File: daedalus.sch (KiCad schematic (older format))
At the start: 106 parts, among them J1 CAN Bus, J2 CAN Bus, J3 I2C 1 Breakout, J4 I2C 1 Breakout, J5 A Terminal, J6 B Terminal, J7 C Terminal, J8 SWD, J9 USB_B_Micro, Q1 AO3401A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

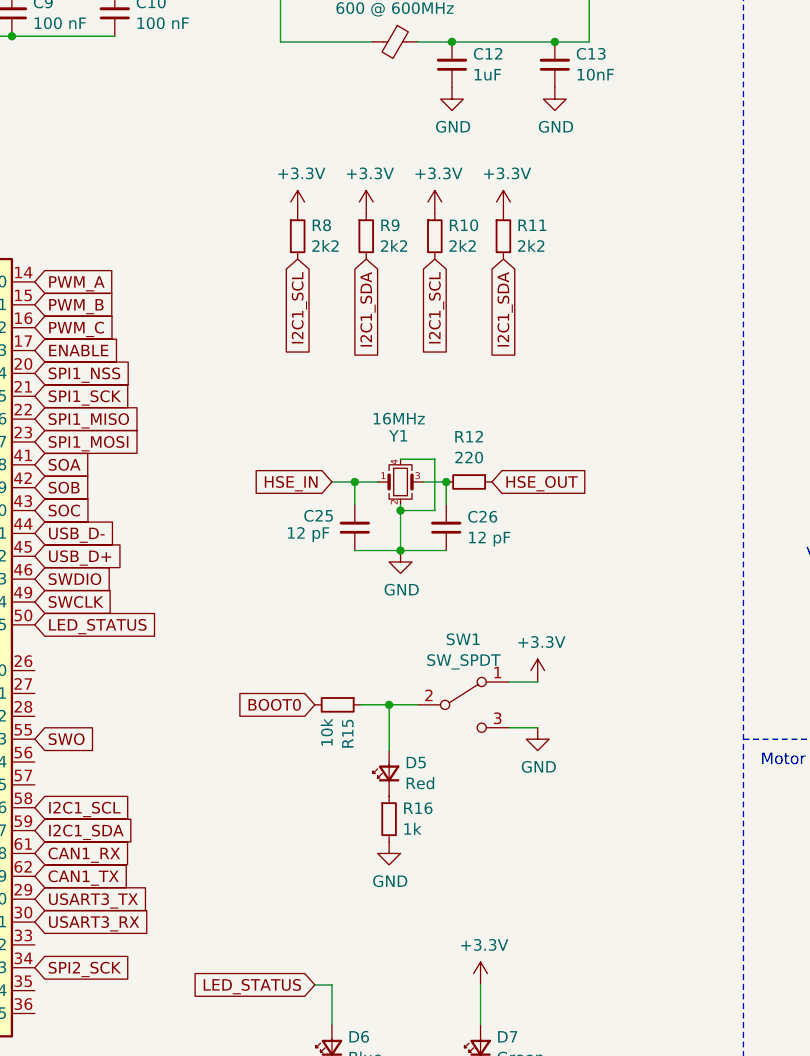
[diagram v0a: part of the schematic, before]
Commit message: Began sample routing, removed boot switch
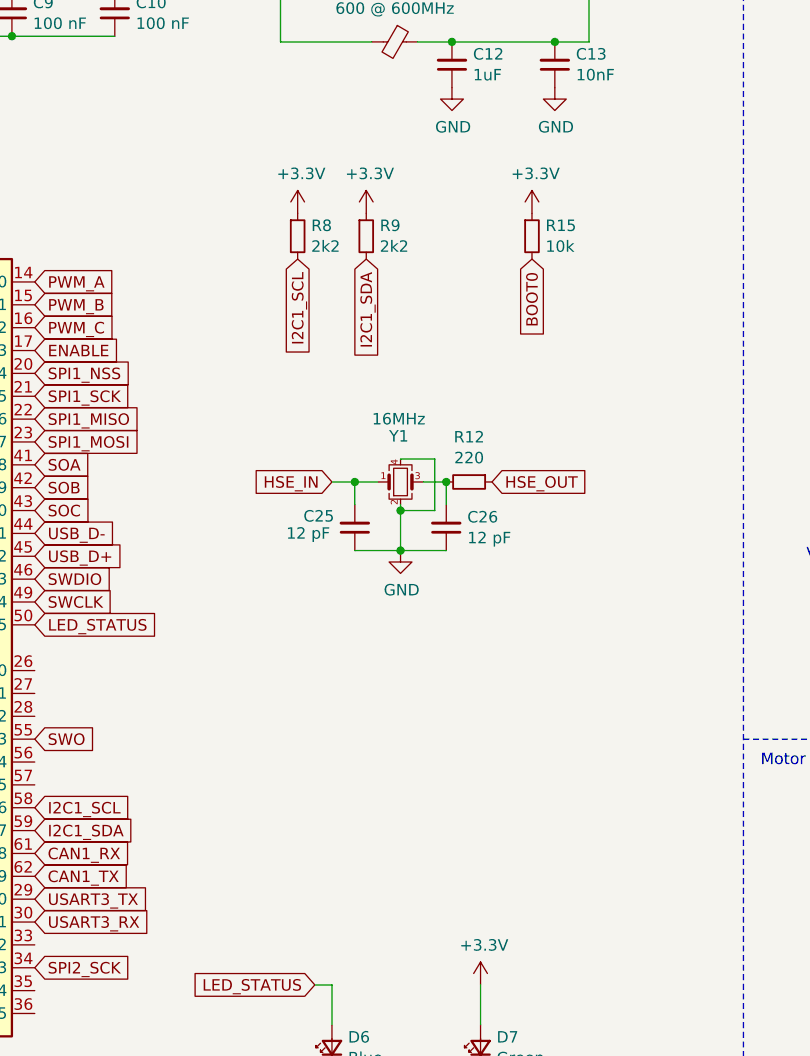
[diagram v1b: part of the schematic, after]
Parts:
- removed D5: Red, LED_SMD:LED_0603_1608Metric, symbol Device:LED_Small
- removed R10, R11: 2k2, Resistor_SMD:R_0402_1005Metric, symbol Device:R_Small
- removed R16: 1k, Resistor_SMD:R_0402_1005Metric, symbol Device:R_Small
- removed SW1: SW_SPDT, Button_Switch_SMD:SW_SPDT_PCM12, symbol Switch:SW_SPDT
- J5, J6, J7: footprint daedalus_kicad_lib:18_AWG_PAD -> Connector_Wire:SolderWire-1sqmm_1x01_D1.4mm_OD2.7mm
- R19, R20, R21: footprint Resistor_SMD:R_0402_1005Metric -> Resistor_SMD:R_1206_3216Metric
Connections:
- net +3V3: now also R15.1
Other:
- moved on the sheet: R15
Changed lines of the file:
@@
 	2000 7075 2000 7175
 Connection ~ 2000 7075
-Text GLabel 4025 5525 0    50   Input ~ 0
+Text GLabel 4975 3575 3    50   Input ~ 0
 BOOT0
 $Comp
 L Device:R_Small R15
 U 1 1 6026C4AC
-P 4125 5525
-F 0 "R15" H 4184 5571 50  0000 L CNN
-F 1 "10k" H 4184 5480 50  0000 L CNN
-F 2 "Resistor_SMD:R_0402_1005Metric" H 4125 5525 50  0001 C CNN
-F 3 "~" H 4125 5525 50  0001 C CNN
-F 4 "C25744" H 4125 5525 50  0001 C CNN "LCSC Part #"
-	1    4125 5525
-	0    1    1    0
+P 4975 3475
+F 0 "R15" H 5034 3521 50  0000 L CNN
+F 1 "10k" H 5034 3430 50  0000 L CNN
+F 2 "Resistor_SMD:R_0402_1005Metric" H 4975 3475 50  0001 C CNN
+F 3 "~" H 4975 3475 50  0001 C CNN
+F 4 "C25744" H 4975 3475 50  0001 C CNN "LCSC Part #"
+	1    4975 3475
+	1    0    0    -1
 $EndComp
 Text GLabel 3950 3575 3    50   Input ~ 0
@@
 $EndComp
 $Comp
-L Switch:SW_SPDT SW1
-U 1 1 603683AC
-P 4675 5525
-F 0 "SW1" H 4675 5810 50  0000 C CNN
-F 1 "SW_SPDT" H 4675 5719 50  0000 C CNN
-F 2 "Button_Switch_SMD:SW_SPDT_PCM12" H 4675 5525 50  0001 C CNN
-F 3 "~" H 4675 5525 50  0001 C CNN
-	1    4675 5525
-	1    0    0    -1
-$EndComp
-$Comp
 L power:+3.3V #PWR053
 U 1 1 6037937D
-P 5000 5425
-F 0 "#PWR053" H 5000 5275 50  0001 C CNN
-F 1 "+3.3V" H 5015 5598 50  0000 C CNN
-F 2 "" H 5000 5425 50  0001 C CNN
-F 3 "" H 5000 5425 50  0001 C CNN
-	1    5000 5425
-	1    0    0    -1
-$EndComp
-$Comp
-L power:GND #PWR054
-U 1 1 6037A35B
-P 5000 5625
-F 0 "#PWR054" H 5000 5375 50  0001 C CNN
-F 1 "GND" H 5005 5452 50  0000 C CNN
-F 2 "" H 5000 5625 50  0001 C CNN
-F 3 "" H 5000 5625 50  0001 C CNN
-	1    5000 5625
-	1    0    0    -1
-$EndComp
-Wire Wire Line
-	4875 5425 5000 5425
-Wire Wire Line
-	5000 5625 4875 5625
-$Comp
-L Device:LED_Small D5
-U 1 1 603A1483
-P 4350 5825
-F 0 "D5" V 4396 5755 50  0000 R CNN
-F 1 "Red" V 4305 5755 50  0000 R CNN
-F 2 "LED_SMD:LED_0603_1608Metric" V 4350 5825 50  0001 C CNN
-F 3 "~" V 4350 5825 50  0001 C CNN
-F 4 "C2286" H 4350 5825 50  0001 C CNN "LCSC Part #"
-	1    4350 5825
-	0    -1   -1   0
+P 4975 3375
+F 0 "#PWR053" H 4975 3225 50  0001 C CNN
+F 1 "+3.3V" H 4990 3548 50  0000 C CNN
+F 2 "" H 4975 3375 50  0001 C CNN
+F 3 "" H 4975 3375 50  0001 C CNN
+	1    4975 3375
+	1    0    0    -1
 $EndComp
 $Comp
@@
 Text Notes 525  7925 0    50   ~ 0
 Programming / Debug Interfaces
-Wire Wire Line
-	4225 5525 4350 5525
-Wire Wire Line
-	4350 5725 4350 5525
-Connection ~ 4350 5525
-Wire Wire Line
-	4350 5525 4475 5525
-$Comp
-L Device:R_Small R16
-U 1 1 6041D289
-P 4350 6025
-F 0 "R16" H 4409 6071 50  0000 L CNN
-F 1 "1k" H 4409 5980 50  0000 L CNN
-F 2 "Resistor_SMD:R_0402_1005Metric" H 4350 6025 50  0001 C CNN
-F 3 "~" H 4350 6025 50  0001 C CNN
-F 4 "C25744" H 4350 6025 50  0001 C CNN "LCSC Part #"
-	1    4350 6025
-	1    0    0    -1
-$EndComp
-$Comp
-L power:GND #PWR057
-U 1 1 6041DC53
-P 4350 6125
-F 0 "#PWR057" H 4350 5875 50  0001 C CNN
-F 1 "GND" H 4355 5952 50  0000 C CNN
-F 2 "" H 4350 6125 50  0001 C CNN
-F 3 "" H 4350 6125 50  0001 C CNN
-	1    4350 6125
-	1    0    0    -1
-$EndComp
 Wire Notes Line
 	9750 2000 9750 475
@@
 F 0 "J5" H 7955 6942 50  0000 L CNN
 F 1 "A Terminal" H 7955 6851 50  0000 L CNN
-F 2 "daedalus_kicad_lib:18_AWG_PAD" H 7875 6900 50  0001 C CNN
+F 2 "Connector_Wire:SolderWire-1sqmm_1x01_D1.4mm_OD2.7mm" H 7875 6900 50  0001 C CNN
 F 3 "~" H 7875 6900 50  0001 C CNN
 	1    7875 6900
@@
 F 0 "R19" H 7684 7996 50  0000 L CNN
 F 1 "0.001" H 7684 7905 50  0000 L CNN
-F 2 "Resistor_SMD:R_0402_1005Metric" H 7625 7950 50  0001 C CNN
+F 2 "Resistor_SMD:R_1206_3216Metric" H 7625 7950 50  0001 C CNN
 F 3 "~" H 7625 7950 50  0001 C CNN
 	1    7625 7950
@@
 F 0 "J6" H 9280 6942 50  0000 L CNN
 F 1 "B Terminal" H 9280 6851 50  0000 L CNN
-F 2 "daedalus_kicad_lib:18_AWG_PAD" H 9200 6900 50  0001 C CNN
+F 2 "Connector_Wire:SolderWire-1sqmm_1x01_D1.4mm_OD2.7mm" H 9200 6900 50  0001 C CNN
 F 3 "~" H 9200 6900 50  0001 C CNN
 	1    9200 6900
@@
 F 0 "R20" H 9009 7996 50  0000 L CNN
 F 1 "0.001" H 9009 7905 50  0000 L CNN
-F 2 "Resistor_SMD:R_0402_1005Metric" H 8950 7950 50  0001 C CNN
+F 2 "Resistor_SMD:R_1206_3216Metric" H 8950 7950 50  0001 C CNN
 F 3 "~" H 8950 7950 50  0001 C CNN
 	1    8950 7950
@@
 F 0 "J7" H 10580 6942 50  0000 L CNN
 F 1 "C Terminal" H 10580 6851 50  0000 L CNN
-F 2 "daedalus_kicad_lib:18_AWG_PAD" H 10500 6900 50  0001 C CNN
+F 2 "Connector_Wire:SolderWire-1sqmm_1x01_D1.4mm_OD2.7mm" H 10500 6900 50  0001 C CNN
 F 3 "~" H 10500 6900 50  0001 C CNN
 	1    10500 6900
@@
 F 0 "R21" H 10309 7996 50  0000 L CNN
 F 1 "0.001" H 10309 7905 50  0000 L CNN
-F 2 "Resistor_SMD:R_0402_1005Metric" H 10250 7950 50  0001 C CNN
+F 2 "Resistor_SMD:R_1206_3216Metric" H 10250 7950 50  0001 C CNN
 F 3 "~" H 10250 7950 50  0001 C CNN
 	1    10250 7950
@@
 Text Notes 8350 10350 0    50   ~ 0
 Caps for Input voltage and leading to MOSFETS
-Text GLabel 4550 3575 3    50   Input ~ 0
-I2C1_SCL
-$Comp
-L Device:R_Small R10
-U 1 1 60568CCC
-P 4550 3475
-F 0 "R10" H 4609 3521 50  0000 L CNN
-F 1 "2k2" H 4609 3430 50  0000 L CNN
-F 2 "Resistor_SMD:R_0402_1005Metric" H 4550 3475 50  0001 C CNN
-F 3 "~" H 4550 3475 50  0001 C CNN
-F 4 "C25879" H 4550 3475 50  0001 C CNN "LCSC Part #"
-	1    4550 3475
-	1    0    0    -1
-$EndComp
-$Comp
-L power:+3.3V #PWR033
-U 1 1 60568CD2
-P 4550 3375
-F 0 "#PWR033" H 4550 3225 50  0001 C CNN
-F 1 "+3.3V" H 4565 3548 50  0000 C CNN
-F 2 "" H 4550 3375 50  0001 C CNN
-F 3 "" H 4550 3375 50  0001 C CNN
-	1    4550 3375
-	1    0    0    -1
-$EndComp
-$Comp
-L Device:R_Small R11
-U 1 1 60568CD9
-P 4850 3475
-F 0 "R11" H 4909 3521 50  0000 L CNN
-F 1 "2k2" H 4909 3430 50  0000 L CNN
-F 2 "Resistor_SMD:R_0402_1005Metric" H 4850 3475 50  0001 C CNN
-F 3 "~" H 4850 3475 50  0001 C CNN
-F 4 "C25879" H 4850 3475 50  0001 C CNN "LCSC Part #"
-	1    4850 3475
-	1    0    0    -1
-$EndComp
-$Comp
-L power:+3.3V #PWR034
-U 1 1 60568CDF
-P 4850 3375
-F 0 "#PWR034" H 4850 3225 50  0001 C CNN
-F 1 "+3.3V" H 4865 3548 50  0000 C CNN
-F 2 "" H 4850 3375 50  0001 C CNN
-F 3 "" H 4850 3375 50  0001 C CNN
-	1    4850 3375
-	1    0    0    -1
-$EndComp
-Text GLabel 4850 3575 3    50   Input ~ 0
-I2C1_SDA
 $EndSCHEMATC

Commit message: Updated footprint and routing
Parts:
- removed J3, J4: I2C 1 Breakout, Connector_JST:JST_PH_S4B-PH-K_1x04_P2.00mm_Horizontal, symbol Connector_Generic:Conn_01x04
- J1, J2: footprint Connector_JST:JST_PH_S3B-PH-K_1x03_P2.00mm_Horizontal -> Connector_JST:JST_PH_S3B-PH-SM4-TB_1x03-1MP_P2.00mm_Horizontal
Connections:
- net PWM_A: now also U7.16 (PA2); no longer U7.14 (PA0)
- net PWM_C: now also U7.14 (PA0); no longer U7.16 (PA2)
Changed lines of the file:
@@
 Text Notes 9800 575  0    50   ~ 0
 Power and Mounting Points
-$Comp
-L Connector_Generic:Conn_01x04 J3
-U 1 1 6033D355
-P 13500 6600
-F 0 "J3" H 13580 6592 50  0000 L CNN
-F 1 "I2C 1 Breakout" H 13580 6501 50  0000 L CNN
-F 2 "Connector_JST:JST_PH_S4B-PH-K_1x04_P2.00mm_Horizontal" H 13500 6600 50  0001 C CNN
-F 3 "~" H 13500 6600 50  0001 C CNN
-	1    13500 6600
-	1    0    0    -1
-$EndComp
-Text GLabel 13300 6700 0    50   Input ~ 0
-I2C1_SDA
-Text GLabel 13300 6800 0    50   Input ~ 0
-I2C1_SCL
-$Comp
-L power:GND #PWR061
-U 1 1 60342267
-P 13300 6500
-F 0 "#PWR061" H 13300 6250 50  0001 C CNN
-F 1 "GND" H 13305 6327 50  0000 C CNN
-F 2 "" H 13300 6500 50  0001 C CNN
-F 3 "" H 13300 6500 50  0001 C CNN
-	1    13300 6500
-	-1   0    0    1
-$EndComp
-$Comp
-L power:+3.3V #PWR063
-U 1 1 60343CEB
-P 13100 6600
-F 0 "#PWR063" H 13100 6450 50  0001 C CNN
-F 1 "+3.3V" H 13115 6773 50  0000 C CNN
-F 2 "" H 13100 6600 50  0001 C CNN
-F 3 "" H 13100 6600 50  0001 C CNN
-	1    13100 6600
-	1    0    0    -1
-$EndComp
-Wire Wire Line
-	13100 6600 13300 6600
 Text GLabel 2800 4175 2    50   Input ~ 0
 SPI1_SCK
@@
 Text GLabel 2800 6675 2    50   Input ~ 0
 SPI2_SCK
-Text GLabel 2800 3675 2    50   Input ~ 0
+Text GLabel 2800 3875 2    50   Input ~ 0
 PWM_A
 Text GLabel 2800 3775 2    50   Input ~ 0
 PWM_B
-Text GLabel 2800 3875 2    50   Input ~ 0
+Text GLabel 2800 3675 2    50   Input ~ 0
 PWM_C
 Text GLabel 2800 3975 2    50   Input ~ 0
@@
 F 0 "J1" H 13580 5717 50  0000 L CNN
 F 1 "CAN Bus" H 13580 5626 50  0000 L CNN
-F 2 "Connector_JST:JST_PH_S3B-PH-K_1x03_P2.00mm_Horizontal" H 13500 5675 50  0001 C CNN
+F 2 "Connector_JST:JST_PH_S3B-PH-SM4-TB_1x03-1MP_P2.00mm_Horizontal" H 13500 5675 50  0001 C CNN
 F 3 "~" H 13500 5675 50  0001 C CNN
 	1    13500 5675
@@
 F 0 "J2" H 15330 5717 50  0000 L CNN
 F 1 "CAN Bus" H 15330 5626 50  0000 L CNN
-F 2 "Connector_JST:JST_PH_S3B-PH-K_1x03_P2.00mm_Horizontal" H 15250 5675 50  0001 C CNN
+F 2 "Connector_JST:JST_PH_S3B-PH-SM4-TB_1x03-1MP_P2.00mm_Horizontal" H 15250 5675 50  0001 C CNN
 F 3 "~" H 15250 5675 50  0001 C CNN
 	1    15250 5675
@@
 Text Notes 12475 1825 0    50   ~ 0
 Two XT30 plugs: power in and daisy chaining
-$Comp
-L Connector_Generic:Conn_01x04 J4
-U 1 1 603C1235
-P 15250 6600
-F 0 "J4" H 15330 6592 50  0000 L CNN
-F 1 "I2C 1 Breakout" H 15330 6501 50  0000 L CNN
-F 2 "Connector_JST:JST_PH_S4B-PH-K_1x04_P2.00mm_Horizontal" H 15250 6600 50  0001 C CNN
-F 3 "~" H 15250 6600 50  0001 C CNN
-	1    15250 6600
-	1    0    0    -1
-$EndComp
-Text GLabel 15050 6700 0    50   Input ~ 0
-I2C1_SDA
-Text GLabel 15050 6800 0    50   Input ~ 0
-I2C1_SCL
-$Comp
-L power:GND #PWR062
-U 1 1 603C123D
-P 15050 6500
-F 0 "#PWR062" H 15050 6250 50  0001 C CNN
-F 1 "GND" H 15055 6327 50  0000 C CNN
-F 2 "" H 15050 6500 50  0001 C CNN
-F 3 "" H 15050 6500 50  0001 C CNN
-	1    15050 6500
-	-1   0    0    1
-$EndComp
-$Comp
-L power:+3.3V #PWR064
-U 1 1 603C1243
-P 14850 6600
-F 0 "#PWR064" H 14850 6450 50  0001 C CNN
-F 1 "+3.3V" H 14865 6773 50  0000 C CNN
-F 2 "" H 14850 6600 50  0001 C CNN
-F 3 "" H 14850 6600 50  0001 C CNN
-	1    14850 6600
-	1    0    0    -1
-$EndComp
-Wire Wire Line
-	14850 6600 15050 6600
 Text Notes 13050 5450 0    50   ~ 0
 2x all busses: input and daisy chain

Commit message: Updated schematic, began v3 layout
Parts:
- removed C14: 10uF 50V, Capacitor_SMD:C_1206_3216Metric, symbol Device:C_Small
- removed J8: SWD, Connector_PinHeader_1.27mm:PinHeader_2x05_P1.27mm_Vertical_SMD, symbol Connector_Generic:Conn_02x05_Odd_Even
- removed U4: MA700, daedalus_kicad_lib:QFN16, symbol ma700:MA700
- added 1: AS5147, daedalus_kicad_lib:TSSOP14_as5147, symbol as5147:AS5147
- added SWD1: Conn_01x06, Connector_JST:JST_PH_S6B-PH-K_1x06_P2.00mm_Horizontal, symbol Connector_Generic:Conn_01x06
- C15: value 0.1 uF 50V -> 0.47uF, 50V
- C28, C29, C30, C31, C32, C33, C34, C35, C36, C37, C38, C39, C40, C41, C42, C43: footprint Capacitor_SMD:C_1206_3216Metric -> Capacitor_SMD:C_0805_2012Metric
- H1, H2, H3, H4: footprint MountingHole:MountingHole_2.7mm_M2.5_Pad -> MountingHole:MountingHole_2.7mm_M2.5_DIN965_Pad
- J5, J6, J7: footprint Connector_Wire:SolderWire-1sqmm_1x01_D1.4mm_OD2.7mm -> TestPoint:TestPoint_Pad_3.0x3.0mm
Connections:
- net +3V3: now also C11.2, 1.12 (VDD3V), SWD1.1 (Pin_1); no longer C11.1
- net GND: now also C11.1, 1.13 (GND), 1.5 (TEST), SWD1.6 (Pin_6); no longer C11.2
- net NRST: now also SWD1.5 (Pin_5)
- net SPI2_CS: now also 1.1 (CS/)
- net SPI2_MISO: now also 1.3 (MISO)
- net SPI2_MOSI: now also 1.4 (MOSI)
- net SWCLK: now also SWD1.4 (Pin_4)
- net SWDIO: now also SWD1.3 (Pin_3)
- net SWO: now also SWD1.2 (Pin_2)
- new net ENC_A: 1.7 (A)
- new net ENC_B: 1.6 (B)
- no-connect marks 14 -> 7
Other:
- note removed: "MA700GQ"
- moved on the sheet: C23, C24, J1, J2, R15

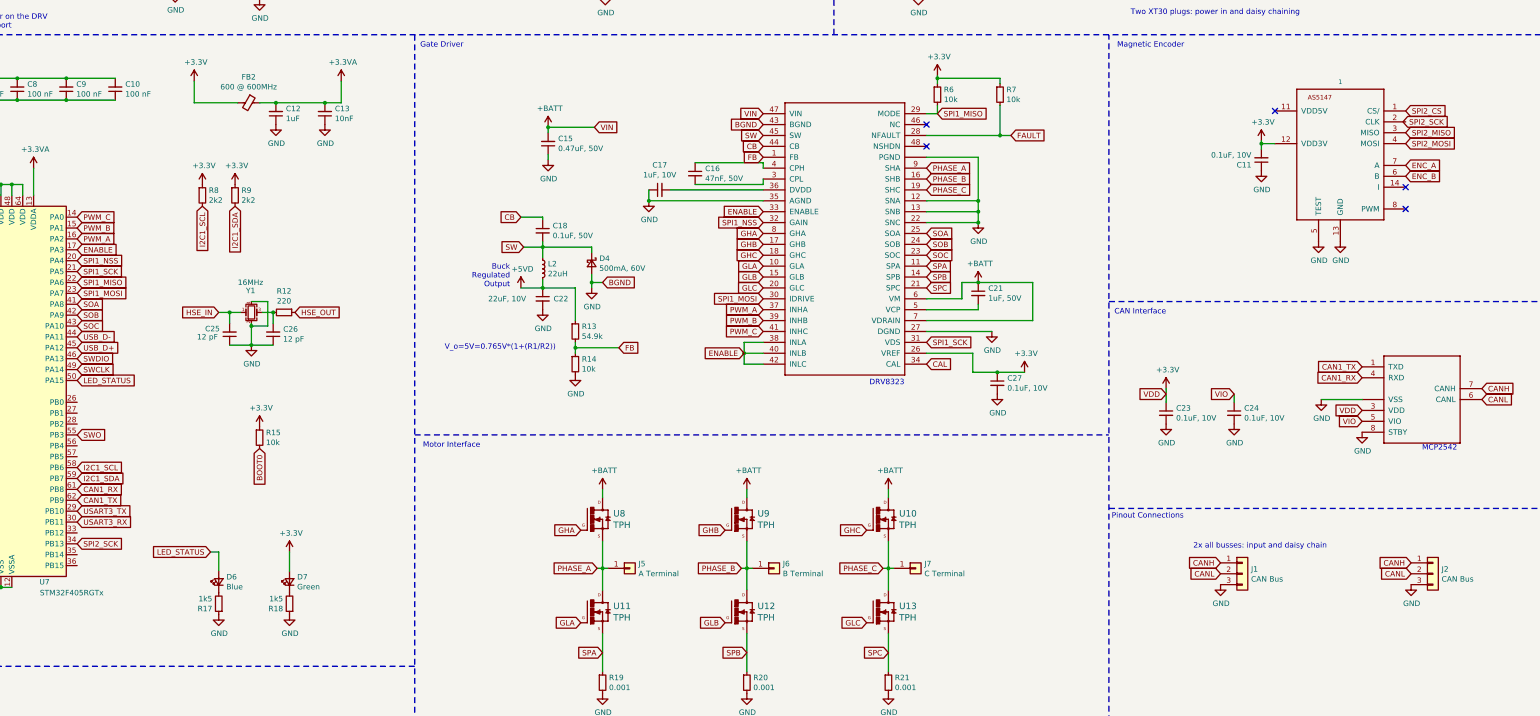
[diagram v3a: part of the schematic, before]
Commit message: Added 5V LED, finished standard routes; about to start pours
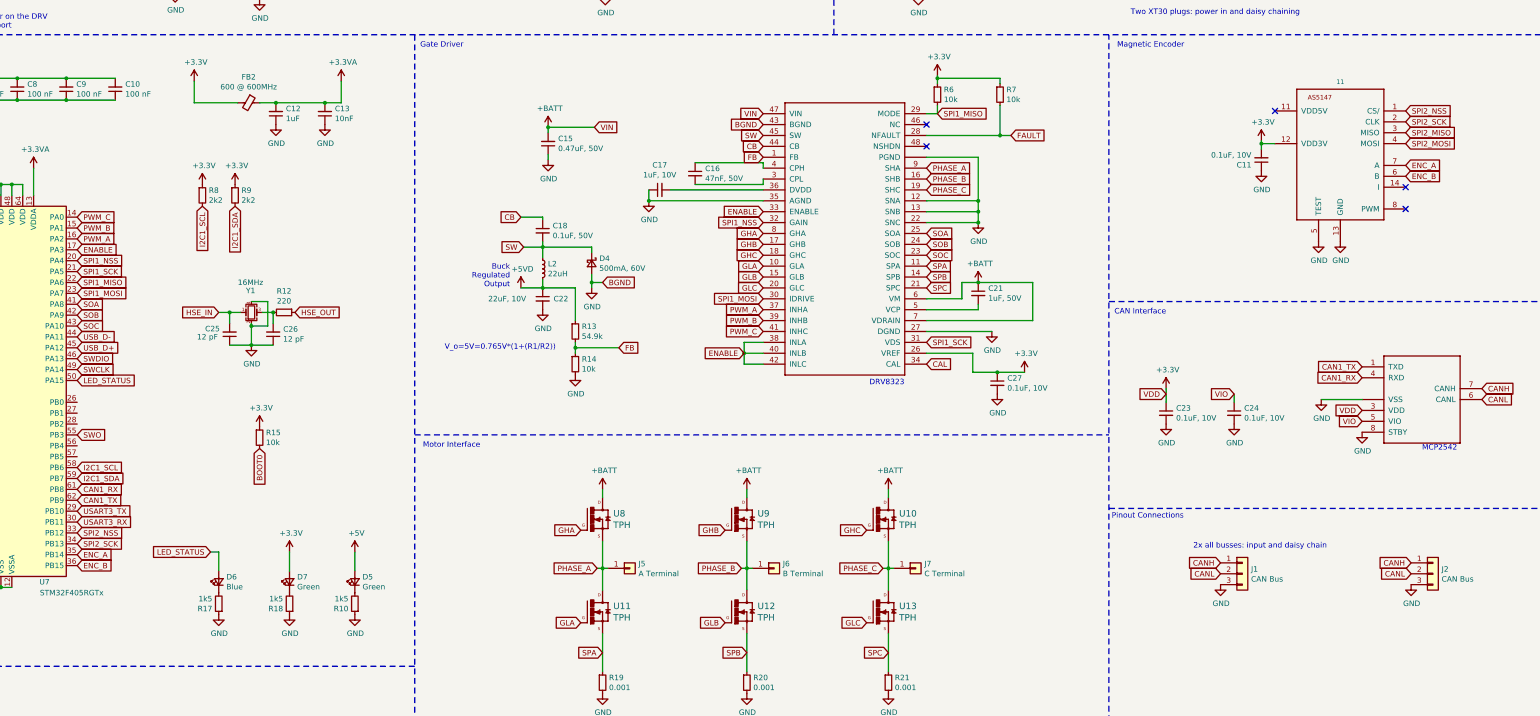
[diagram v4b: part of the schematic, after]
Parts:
- added D5: Green, LED_SMD:LED_0603_1608Metric, symbol Device:LED_Small
- added R10: 1k5, Resistor_SMD:R_0402_1005Metric, symbol Device:R_Small
- renumbered 1 to 11
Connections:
- net SPI2_CS is gone; now on net SPI2_NSS: 11.1 (CS/)
- net +5V: now also D5.2 (A)
- net ENC_A: now also U7.35 (PB14)
- net ENC_B: now also U7.36 (PB15)
- net GND: now also R10.1
- net SPI2_SCK: now also 11.2 (CLK)
- net SPI2_NSS: now reaches U7.33 (PB12)
- new net: D5.1 (K), R10.2
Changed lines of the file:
@@
 NRST
 $Comp
-L as5147:AS5147 1
+L as5147:AS5147 11
 U 1 1 60403972
 P 14400 3100
-F 0 "1" H 14400 3767 42  0000 C CNN
+F 0 "11" H 14400 3767 42  0000 C CNN
 F 1 "AS5147" H 14400 3100 50  0001 C CNN
 F 2 "daedalus_kicad_lib:TSSOP14_as5147" H 14400 3100 50  0001 C CNN
@@
 $EndComp
 Text GLabel 15000 2700 2    50   Input ~ 0
-SPI2_CS
-Text GLabel 14975 2800 2    50   Input ~ 0
+SPI2_NSS
+Text GLabel 15000 2800 2    50   Input ~ 0
 SPI2_SCK
 Text GLabel 15000 2900 2    50   Input ~ 0
@@
 	1    0    0    -1
 $EndComp
+Text GLabel 2800 6575 2    50   Input ~ 0
+SPI2_NSS
+Text GLabel 2800 6775 2    50   Input ~ 0
+ENC_A
+Text GLabel 2800 6875 2    50   Input ~ 0
+ENC_B
+$Comp
+L Device:R_Small R10
+U 1 1 60860FCF
+P 5350 7225
+F 0 "R10" H 5409 7271 50  0000 L CNN
+F 1 "1k5" H 5409 7180 50  0000 L CNN
+F 2 "Resistor_SMD:R_0402_1005Metric" H 5350 7225 50  0001 C CNN
+F 3 "~" H 5350 7225 50  0001 C CNN
+F 4 "C25867" H 5350 7225 50  0001 C CNN "LCSC Part #"
+	1    5350 7225
+	-1   0    0    1
+$EndComp
+$Comp
+L power:GND #PWR0107
+U 1 1 60860FD5
+P 5350 7325
+F 0 "#PWR0107" H 5350 7075 50  0001 C CNN
+F 1 "GND" H 5355 7152 50  0000 C CNN
+F 2 "" H 5350 7325 50  0001 C CNN
+F 3 "" H 5350 7325 50  0001 C CNN
+	1    5350 7325
+	1    0    0    -1
+$EndComp
+$Comp
+L Device:LED_Small D5
+U 1 1 60860FDC
+P 5350 7025
+F 0 "D5" V 5396 6955 50  0000 R CNN
+F 1 "Green" V 5305 6955 50  0000 R CNN
+F 2 "LED_SMD:LED_0603_1608Metric" V 5350 7025 50  0001 C CNN
+F 3 "~" V 5350 7025 50  0001 C CNN
+F 4 "C2286" H 5350 7025 50  0001 C CNN "LCSC Part #"
+	1    5350 7025
+	0    -1   -1   0
+$EndComp
+Wire Wire Line
+	5350 6750 5350 6925
+$Comp
+L power:+5V #PWR0108
+U 1 1 6086C225
+P 5350 6750
+F 0 "#PWR0108" H 5350 6600 50  0001 C CNN
+F 1 "+5V" H 5365 6923 50  0000 C CNN
+F 2 "" H 5350 6750 50  0001 C CNN
+F 3 "" H 5350 6750 50  0001 C CNN
+	1    5350 6750
+	1    0    0    -1
+$EndComp
